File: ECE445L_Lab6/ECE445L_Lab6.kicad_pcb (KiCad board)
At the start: 2 copper layers, 114.4 x 88.9 mm, 32 parts, among them J1 JTAG, J2 Battery, SW1 Reset, SW2 Input, U1 TM4C123GH6PMIR, U2 Adafruit ST7735R, U3 LP2950-33LPRE3, Y1 ABM3-16.000MHZ-B2-T

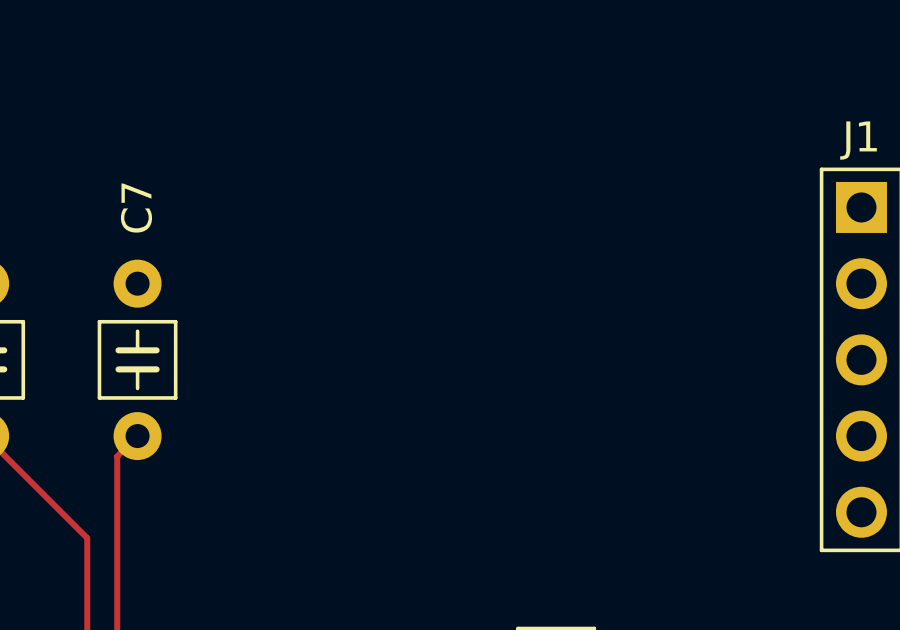
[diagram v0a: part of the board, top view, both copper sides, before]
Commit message: Swap TDI and TDO
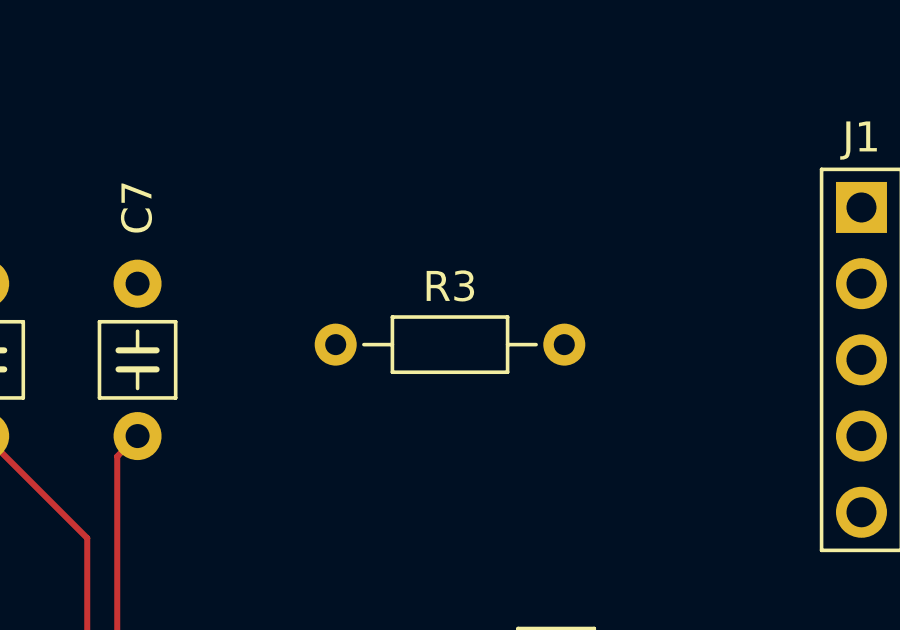
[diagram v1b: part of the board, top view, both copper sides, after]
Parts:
- added R3: 10k, ECE445L:R_Axial_DIN0204_L3.6mm_D1.6mm_P7.62mm_Horizontal, F.Cu at (124.1, 50.9)
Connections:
- J1 pad 4: /TDI -> /TDO
- J1 pad 5: /TDO -> /TDI

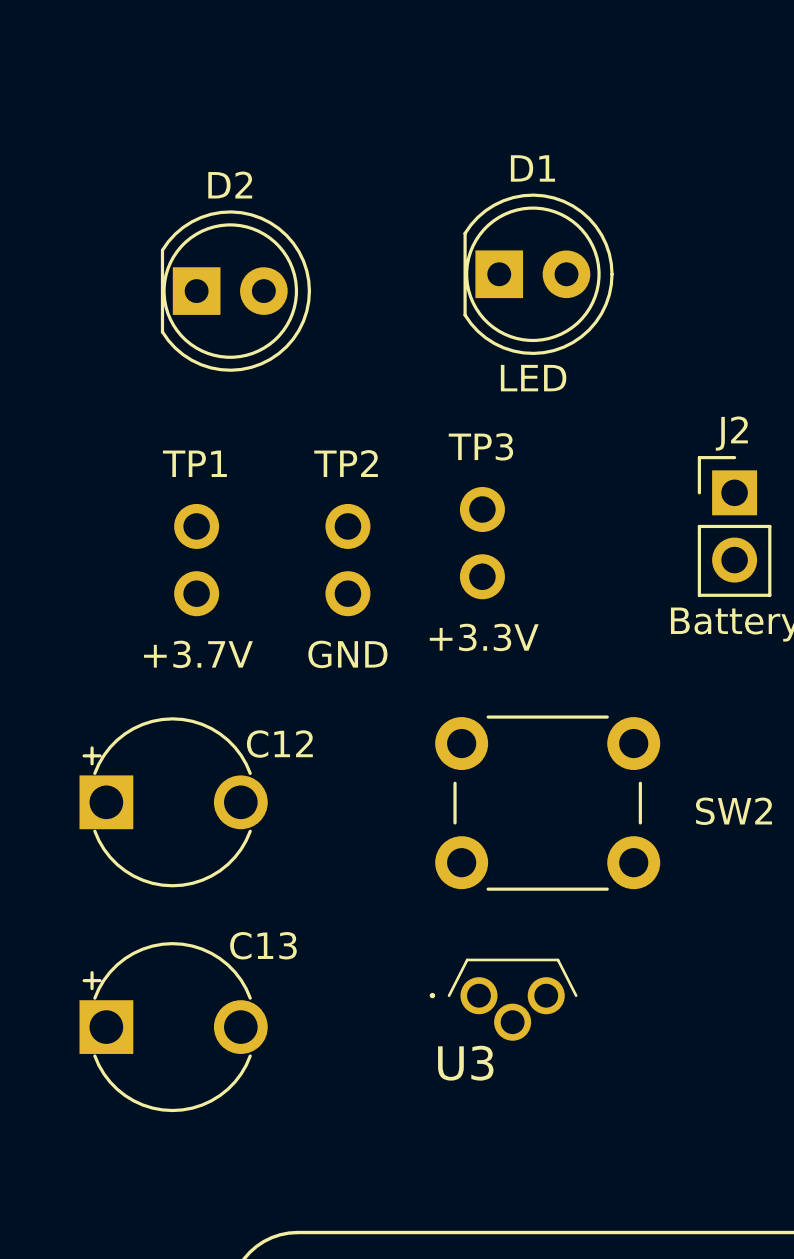
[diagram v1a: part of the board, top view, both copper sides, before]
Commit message: update all symbols and re-sync footprints in the KiCad projects
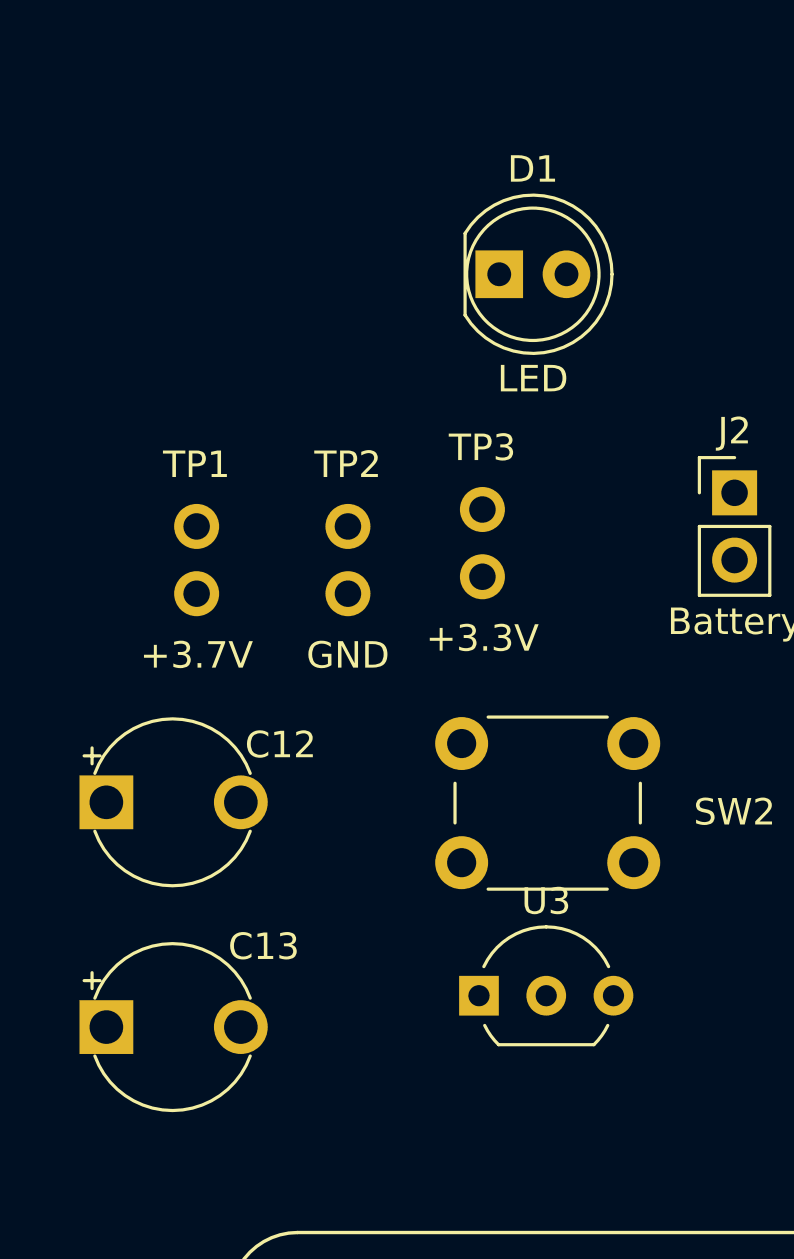
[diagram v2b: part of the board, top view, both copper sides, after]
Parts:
- removed D2: LED, ECE445L:LED_D5.0mm
- U3: footprint ECE445L:TL431CLPM -> Package_TO_SOT_THT:TO-92_Inline_Wide
